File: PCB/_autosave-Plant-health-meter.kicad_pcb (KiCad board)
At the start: 4 copper layers, 136.2 x 25 mm, 104 parts, among them J1 Conn_01x02, J2 Conn_01x02, J3 Conn_01x02, J4 Conn_01x02, J5 USB_C_Receptacle_USB2.0_14P, J6 Conn_01x02, J7 Conn_02x08_Counter_Clockwise, Q1 AO3401A, SW1 Boot, SW2 Reset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

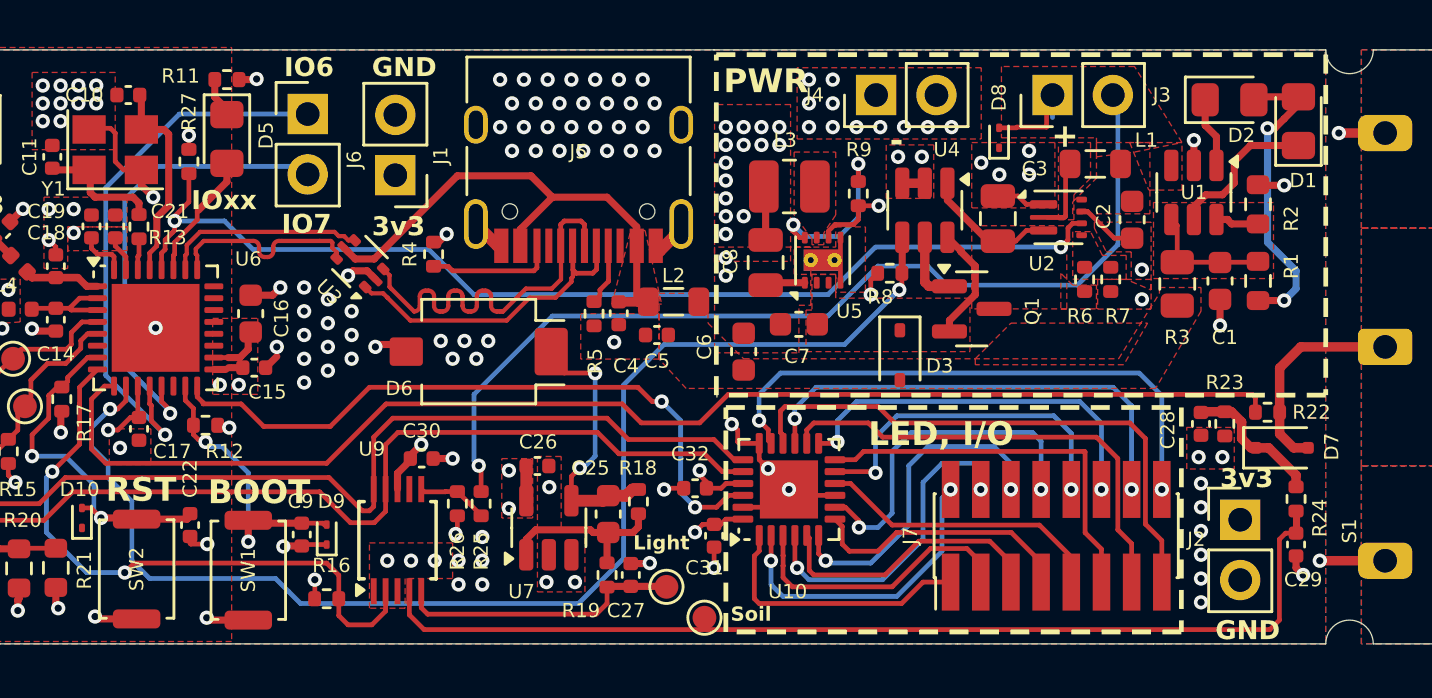
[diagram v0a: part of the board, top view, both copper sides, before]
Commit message: ESD protection and Boost UVLO
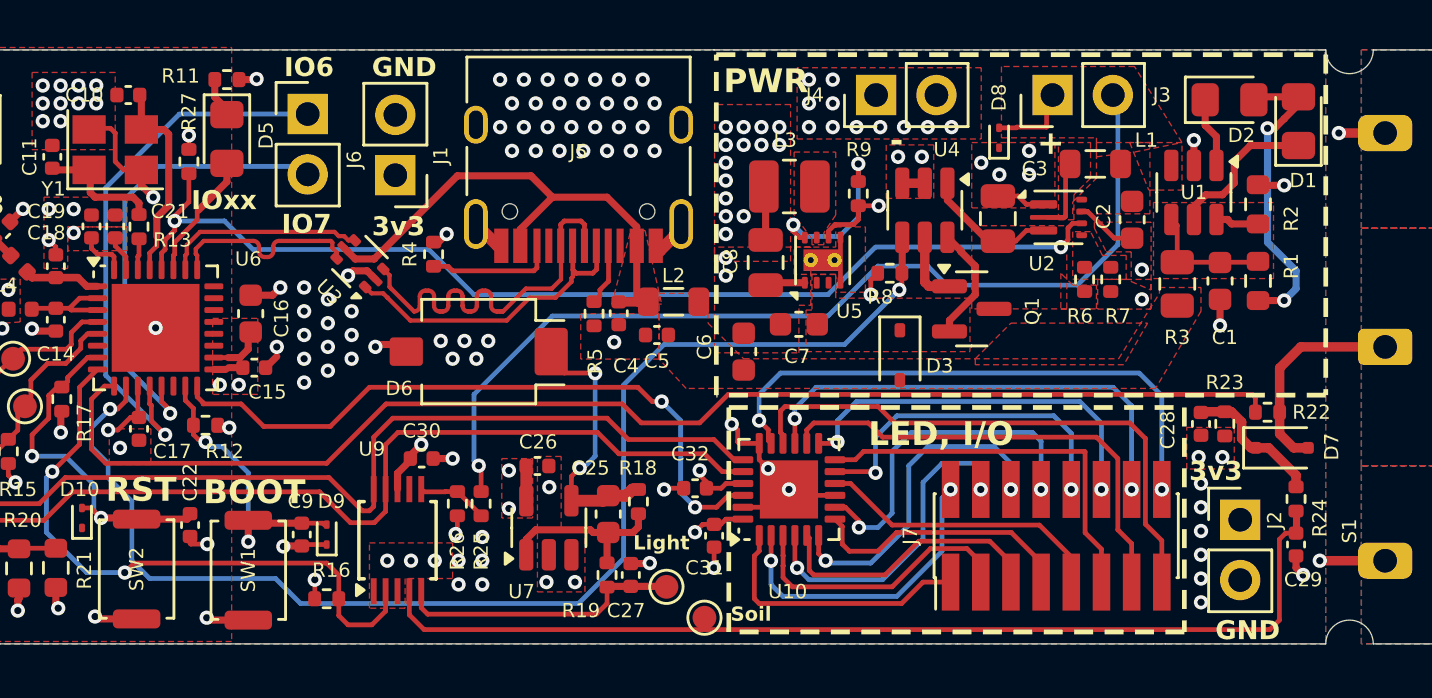
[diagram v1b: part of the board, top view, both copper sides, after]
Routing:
- net +BATT: track 45.4 -> 44.4 mm
